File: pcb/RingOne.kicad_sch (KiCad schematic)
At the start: 23 parts

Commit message: Schema: add power path control, input button and bluetooth module
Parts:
- added BT?: 1S Li-Po, symbol Device:Battery_Cell
- added C? (x2): 4.7uF, symbol Device:C
- added C?: 100nF, symbol Device:C
- added C? (x7): 1uF, symbol Device:C
- added C? (x2): 1uF, Capacitor_SMD:C_0603_1608Metric, symbol Device:C
- added C?: 100nF, Capacitor_SMD:C_0603_1608Metric, symbol Device:C
- added D?: 3V3, Diode_SMD:D_SOD-523, symbol Device:D_Zener
- added D? (x2): D_Schottky, symbol Device:D_Schottky
- added D?: EADA25L, symbol Device:D_Schottky_Dual_CommonAnode_KKA
- added J?: PROG_CONN, TCY_connectors:Amphenol_10114828-11103LF_1x03_P1.25mm_Vertical, symbol Connector_Generic:Conn_01x03
- added J?: DBG_UART, TCY_connectors:Amphenol_10114828-11103LF_1x03_P1.25mm_Vertical, symbol Connector_Generic:Conn_01x03
- added Q? (x2): YJQ3400, TCY_IC:UDFN-6-2EP_2x2mm_P0.65mm_EP1x0.7mm, symbol TCY_transistors:YJQ3400
- added R? (x2): 10k, symbol Device:R
- added R? (x2): 1k, symbol Device:R
- added R? (x2): R, symbol Device:R
- added R?: 2k2, symbol Device:R
- added R?: 22k, symbol Device:R
- added SW?: WAKEUP, TCY_buttons_switches:EVQ-P7J01P, symbol Switch:SW_Push_Dual
- added SW?: BOOT, TCY_buttons_switches:KMT031NGJLHS, symbol Switch:SW_Push_Dual
- added U?: MIC94300, TCY_IC:MLF-4_1.2x1.6mm_P0.5_1EP_0.85x0.5mm, symbol TCY_IC:MIC94300
- added U? (x2): LM66100, Package_TO_SOT_SMD:SOT-363_SC-70-6, symbol TCY_power_management:LM66100
- added U? (x2): PMDPB70XP, TCY_IC:UDFN-6-2EP_2x2mm_P0.65mm_EP1x0.7mm, symbol TCY_transistors:PMDPB70XP
- added U?: MCP73831-2-OT, Package_TO_SOT_SMD:SOT-23-5, symbol Battery_Management:MCP73831-2-OT
- added U?: RN4871, RF_Module:Microchip_RN4871, symbol RF_Bluetooth:RN4871
- added U?: BQ297xy, Package_SON:WSON-6_1.5x1.5mm_P0.5mm, symbol Battery_Management:BQ297xy
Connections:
- net +3V3: now also U?.22 (VSYS), C?.1, C?.1, U?.14 (VBAT)
- net GND: now also U?.10 (GND), U?.13 (ADDR0), U?.25 (EP), U?.3 (VCONN), U?.4 (GND), U?.9 (EPAD), C?.2, C?.2, C?.2, C?.2, C?.2, C?.2, C?.2, C?.2, C?.2, C?.2, C?.2, C?.2, D?.2 (A), D?.3 (A), J?.1 (Pin_1), J?.1 (Pin_1), Q?.4 (S2), R?.2, R?.2, R?.2, R?.2, SW?.1, SW?.1, SW?.3, SW?.3, U?.13 (GND), U?.2 (GND), U?.2 (GND), U?.2 (GND), U?.2 (GND), U?.2 (VSS), U?.5 (E_PAD)
- net RESET: now also U?.10 (RST)
- net SCL: now also U?.8 (SDA)
- net SDA: now also U?.7 (SCL)
- net VBUS: now also U?.18 (VBUS_SENSE), C?.1, C?.1, U?.6, U?.7
- net CC1: now reaches U?.1 (CC1DB)
- net CC1: now also J?.A5 (CC1), U?.2 (CC1), D?.1 (K)
- net USB_VALID: now reaches U?.11 (VBUS_VALID)
- net USB_ATTACH: now reaches U?.12 (ATTACH)
- net USB_DEBUG: now reaches U?.14 (DEBUG1)
- net at U?.19 (VBUS_EN_SINK): now also R?.2
- net at U?.21 (VREG_1V2): now also C?.1
- net at U?.23 (VREG_2V7): now also C?.1
- net CC2: now reaches U?.4 (CC2)
- net CC2: now also J?.B5 (CC2), U?.5 (CC2DB), D?.2 (K)
- net at U?.6 (RESET): now also R?.1
- net USB_INT: now reaches U?.9 (ALERT#)
- net PWR_EN: now reaches U?.5 (EN)
- net PWR_EN: now also D?.1 (K), D?.1 (K), D?.1 (K), R?.1
- net VCC: now reaches U?.8 (VI)
- net VCC: now also C?.1, C?.1, U?.6 (VOUT), U?.6 (VOUT)
- new net: BT?.2 (-), C?.2, Q?.1 (S), U?.4 (VSS)
- new net: C?.1, R?.2, U?.5 (BAT)
- new net: R?.1, R?.2, U?.2, U?.5
- new net: R?.2, U?.3 (~CE), U?.5 (ST)
- new net: C?.1, U?.3 (VOUT)
- new net: C?.1, U?.4 (VIN)
- new net: R?.1, U?.1, U?.4
- new net: R?.1, U?.6 (V-)
- new net: Q?.2 (G1), U?.3 (Dout)
- new net: Q?.3 (D2), Q?.6 (D2), Q?.7 (D2), Q?.8 (D2)
- new net: Q?.5 (G2), U?.2 (Cout)
- new net: R?.1, U?.5 (PROG)
- new net +5V: C?.1, R?.1, U?.1 (VIN), U?.3, U?.4 (VDD), U?.8
- new net +BATT: BT?.1 (+), C?.1, R?.1, U?.1 (VIN), U?.3 (VBAT), U?.3 (~CE)
- new net BL_RX: U?.8 (UART_TX)
- new net BL_TX: U?.7 (UART_RX)
- new net BTN_Denoise_BOOT/IN: SW?.2, SW?.4
- new net BTN_Denoise_WAKE/IN: SW?.2, SW?.4
- new net DBG_RX: J?.3 (Pin_3)
- new net DBG_TX: J?.2 (Pin_2)
- new net PWR_BTN: D?.2 (A)
- new net PWR_MCU: D?.2 (A)
- new net P_OR: U?.5 (ST)
- new net SWCLK: J?.2 (Pin_2)
- new net SWDIO: J?.3 (Pin_3)
- no-connect marks 3 -> 15
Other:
- added sheet BTN_Denoise_BOOT (BTN_Denoise.kicad_sch)
- added sheet BTN_Denoise_WAKE (BTN_Denoise.kicad_sch)
- note added: "Battery protection"
- note added: "Charging"
- note added: "Charging current: 45 mA"
- note added: "Current sensing"
- note added: "IMU"
- note added: "Input buttons"
- note added: "Power OR-ing"
- note added: "Prog & debug"
- note added: "Use intenal pullup in MCU for: INT, DEBUG, VALID, ATTACH"
- moved on the sheet: C?, D?, FB?, J?, R?, SW?, TP?, U?, U?A

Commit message: Schema: finalization of schematic, break main page into hierarchical
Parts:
- removed BT?: 1S Li-Po, symbol Device:Battery_Cell
- removed C? (x2): 4.7uF, symbol Device:C
- removed C?: 100nF, symbol Device:C
- removed C? (x7): 1uF, symbol Device:C
- removed C? (x2): 1uF, Capacitor_SMD:C_0603_1608Metric, symbol Device:C
- removed C?: 100nF, Capacitor_SMD:C_0603_1608Metric, symbol Device:C
- removed D?: 3V3, Diode_SMD:D_SOD-523, symbol Device:D_Zener
- removed D? (x2): D_Schottky, symbol Device:D_Schottky
- removed D?: EADA25L, symbol Device:D_Schottky_Dual_CommonAnode_KKA
- removed FB?: 50R@100Mhz, Inductor_SMD:L_1206_3216Metric, symbol Device:FerriteBead_Small
- removed J?: USB_C_Receptacle_USB2.0, Connector_USB:USB_C_Receptacle_HRO_TYPE-C-31-M-12, symbol Connector:USB_C_Receptacle_USB2.0
- removed Q? (x2): YJQ3400, TCY_IC:UDFN-6-2EP_2x2mm_P0.65mm_EP1x0.7mm, symbol TCY_transistors:YJQ3400
- removed R? (x2): 10k, symbol Device:R
- removed R? (x2): 1k, symbol Device:R
- removed R? (x2): R, symbol Device:R
- removed R? (x2): 22R, Resistor_SMD:R_0603_1608Metric, symbol Device:R
- removed R?: 2k2, symbol Device:R
- removed R?: 22k, symbol Device:R
- removed SW?: WAKEUP, TCY_buttons_switches:EVQ-P7J01P, symbol Switch:SW_Push_Dual
- removed SW?: BOOT, TCY_buttons_switches:KMT031NGJLHS, symbol Switch:SW_Push_Dual
- removed TP?: VBUS, TCY_connectors:TestPoint_Pad_D0.5mm, symbol Connector:TestPoint
- removed U?: MIC94300, TCY_IC:MLF-4_1.2x1.6mm_P0.5_1EP_0.85x0.5mm, symbol TCY_IC:MIC94300
- removed U? (x2): LM66100, Package_TO_SOT_SMD:SOT-363_SC-70-6, symbol TCY_power_management:LM66100
- removed U? (x2): PMDPB70XP, TCY_IC:UDFN-6-2EP_2x2mm_P0.65mm_EP1x0.7mm, symbol TCY_transistors:PMDPB70XP
- removed U?: USBLC6-2SC6, Package_TO_SOT_SMD:SOT-23-6, symbol Power_Protection:USBLC6-2SC6
- removed U?: MCP73831-2-OT, Package_TO_SOT_SMD:SOT-23-5, symbol Battery_Management:MCP73831-2-OT
- removed U?: STUSB1600AQTR, Package_DFN_QFN:QFN-24-1EP_4x4mm_P0.5mm_EP2.7x2.7mm, symbol TCY_IC:STUSB1600AQTR
- removed U?: BQ297xy, Package_SON:WSON-6_1.5x1.5mm_P0.5mm, symbol Battery_Management:BQ297xy
- removed U?: NCV8165ML330, Package_DFN_QFN:DFN-8-1EP_3x3mm_P0.65mm_EP1.55x2.4mm, symbol TCY_voltage_regulators:NCV8165ML330
- added C1: 10uF, Capacitor_SMD:C_0805_2012Metric, symbol Device:C
- added C2, C3, C4, C5, C6: 100nF, Capacitor_SMD:C_0603_1608Metric, symbol Device:C
- C10, C9: renamed from C?; footprint (none) -> TCY_passives:C_0603_1608Metric
- J1, J2: renamed from J?; footprint TCY_connectors:Amphenol_10114828-11103LF_1x03_P1.25mm_Vertical -> TCY_connectors:Amphenol_10114830-11103LF_1x03_P1.25mm_Horizontal
- U4: renamed from U?; symbol TCY_IC:KTD2026BEWE -> TCY_LEDs:KTD2026BEWE
- gave numbers to parts that had none: 13
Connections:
- net +3V3: now also C1.1, C2.1, C3.1, C4.1, C5.1, C6.1; no longer U1.1 (VBAT)
- net BL_RX: now also U1.13 (PA3)
- net BL_TX: now also U1.12 (PA2)
- net DBG_RX: now also U1.22 (PB11)
- net DBG_TX: now also U1.21 (PB10)
- net GND: now also C1.2, C2.2, C3.2, C4.2, C5.2, C6.2
- net IMU_INT1: now also U1.25 (PB12)
- net IMU_INT2: now also U1.19 (PB1)
- net MISO: now also U1.27 (PB14)
- net MOSI: now also U1.28 (PB15)
- net PWR_BTN: now also U1.10 (PA0)
- net PWR_MCU: now also U1.17 (PA7)
- net RESET: now also U1.7 (NRST)
- net SCK: now also U1.26 (PB13)
- net SCL: now also U1.30 (PA9)
- net SDA: now also U1.31 (PA10)
- net SWCLK: now also U1.37 (PA14)
- net SWDIO: now also U1.34 (PA13)
- net USB_ATTACH: now also U1.40 (PB4)
- net USB_DEBUG: now also U1.42 (PB6)
- net USB_INT: now also U1.20 (PB2)
- net USB_VALID: now also U1.39 (PB3)
- net BAT_V_MON: now reaches U1.14 (PA4)
- net CS_MON: now reaches U1.15 (PA5)
- net BAT_M_EN: now reaches U1.16 (PA6)
- net CS_FLASH: now reaches U1.18 (PB0)
- net CS_FLASH: now also U6.1 (~CS)
- net PER_EN: now reaches U1.2 (PC13)
- net CS_IMU: now reaches U1.29 (PA8)
- net CS_IMU: now also U5.12 (MODE/CS)
- net USB_D+: now reaches U1.32 (PA11)
- net USB_D-: now reaches U1.33 (PA12)
- net PWR_OR: now reaches U1.38 (PA15)
- net CHARG_STAT: now reaches U1.45 (PB8)
- removed net CS: U5.12 (MODE/CS), U6.1 (~CS)
- net LED_PWR renamed PER_PWR
- no-connect marks 15 -> 21
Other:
- removed sheet BTN_Denoise_BOOT
- removed sheet BTN_Denoise_WAKE
- added sheet Battery_management (Battery_management.kicad_sch)
- added sheet Power_management (Power_management.kicad_sch)
- added sheet USB-C (USB-C.kicad_sch)
- note removed: "Battery protection"
- note removed: "Charging"
- note removed: "Charging current: 45 mA"
- note removed: "Current sensing"
- note removed: "Input buttons"
- note removed: "Power OR-ing"
- note removed: "USB type-C input"
- note removed: "Use intenal pullup in MCU for: INT, DEBUG, VALID, ATTACH"
- moved on the sheet: C7, J1, J2, R1, R2, SW1, U1, U2

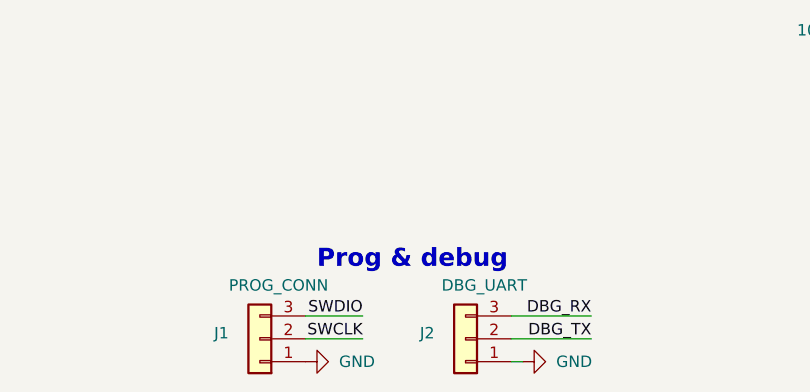
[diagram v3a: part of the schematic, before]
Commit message: PCB: add connection of connector mounting point to ground
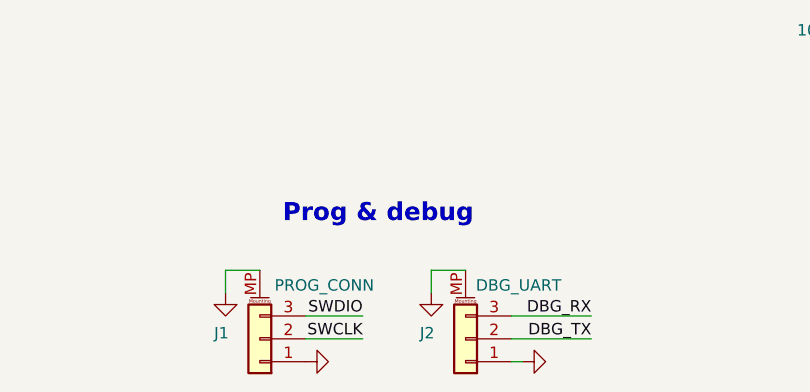
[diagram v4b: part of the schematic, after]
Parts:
- J1, J2: symbol Connector_Generic:Conn_01x03 -> Connector_Generic_MountingPin:Conn_01x03_MountingPin
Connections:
- net GND: now also J1.MP (MountPin), J2.MP (MountPin)
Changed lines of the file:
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@@
+    (stroke (width 0) (type solid) (color 0 0 0 0))
+  )
+  (wire (pts (xy 127 177.8) (xy 130.81 177.8))
+    (stroke (width 0) (type solid) (color 0 0 0 0))
+  )
+  (wire (pts (xy 127 180.34) (xy 127 177.8))
     (stroke (width 0) (type solid) (color 0 0 0 0))
   )
@@
   )
   (wire (pts (xy 149.86 40.64) (xy 149.86 38.1))
+    (stroke (width 0) (type solid) (color 0 0 0 0))
+  )
+  (wire (pts (xy 149.86 177.8) (xy 153.67 177.8))
+    (stroke (width 0) (type solid) (color 0 0 0 0))
+  )
+  (wire (pts (xy 149.86 180.34) (xy 149.86 177.8))
     (stroke (width 0) (type solid) (color 0 0 0 0))
   )
@@
     (stroke (width 0) (type dash) (color 0 0 0 0))
   )
-  (text "Prog & debug" (at 137.16 177.8 0)
+  (text "Prog & debug" (at 133.35 172.72 0)
     (effects (font (size 2 2) (thickness 0.4) bold) (justify left bottom))
   )
@@
     )
   )
+  (symbol (lib_id "power:GND") (at 127 180.34 0) (unit 1)
+    (in_bom yes) (on_board yes)
+    (property "Reference" "#PWR0198" (id 0) (at 127 186.69 0)
+      (effects (font (size 1.27 1.27)) hide)
+    )
+    (property "Value" "GND" (id 1) (at 127 186.055 90)
+      (effects (font (size 1.27 1.27)) hide)
+    )
+    (property "Footprint" "" (id 2) (at 127 180.34 0)
+      (effects (font (size 1.27 1.27)) hide)
+    )
+    (property "Datasheet" "" (id 3) (at 127 180.34 0)
+      (effects (font (size 1.27 1.27)) hide)
+    )
+  )
   (symbol (lib_id "power:GND") (at 135.89 187.96 90) (unit 1)
     (in_bom yes) (on_board yes)
@@
       (effects (font (size 1.27 1.27)) hide)
     )
-    (property "Value" "GND" (id 1) (at 141.605 187.96 90))
+    (property "Value" "GND" (id 1) (at 141.605 187.96 90)
+      (effects (font (size 1.27 1.27)) hide)
+    )
     (property "Footprint" "" (id 2) (at 135.89 187.96 0)
       (effects (font (size 1.27 1.27)) hide)
@@
     )
   )
+  (symbol (lib_id "power:GND") (at 149.86 180.34 0) (unit 1)
+    (in_bom yes) (on_board yes)
+    (property "Reference" "#PWR0197" (id 0) (at 149.86 186.69 0)
+      (effects (font (size 1.27 1.27)) hide)
+    )
+    (property "Value" "GND" (id 1) (at 149.86 186.055 90)
+      (effects (font (size 1.27 1.27)) hide)
+    )
+    (property "Footprint" "" (id 2) (at 149.86 180.34 0)
+      (effects (font (size 1.27 1.27)) hide)
+    )
+    (property "Datasheet" "" (id 3) (at 149.86 180.34 0)
+      (effects (font (size 1.27 1.27)) hide)
+    )
+  )
   (symbol (lib_id "power:GND") (at 160.02 187.96 90) (unit 1)
     (in_bom yes) (on_board yes)
@@
       (effects (font (size 1.27 1.27)) hide)
     )
-    (property "Value" "GND" (id 1) (at 165.735 187.96 90))
+    (property "Value" "GND" (id 1) (at 165.735 187.96 90)
+      (effects (font (size 1.27 1.27)) hide)
+    )
     (property "Footprint" "" (id 2) (at 160.02 187.96 0)
       (effects (font (size 1.27 1.27)) hide)
@@
     )
   )
-  (symbol (lib_id "Connector_Generic:Conn_01x03") (at 130.81 185.42 180) (unit 1)
+  (symbol (lib_id "Connector_Generic_MountingPin:Conn_01x03_MountingPin") (at 130.81 185.42 180) (unit 1)
     (in_bom yes) (on_board yes)
     (property "Reference" "J1" (id 0) (at 126.5428 184.785 0))
-    (property "Value" "PROG_CONN" (id 1) (at 132.893 179.476 0))
+    (property "Value" "PROG_CONN" (id 1) (at 137.973 179.476 0))
     (property "Footprint" "TCY_connectors:Amphenol_10114830-11103LF_1x03_P1.25mm_Horizontal" (id 2) (at 130.81 185.42 0)
       (effects (font (size 1.27 1.27)) hide)
@@
     )
   )
-  (symbol (lib_id "Connector_Generic:Conn_01x03") (at 153.67 185.42 180) (unit 1)
+  (symbol (lib_id "Connector_Generic_MountingPin:Conn_01x03_MountingPin") (at 153.67 185.42 180) (unit 1)
     (in_bom yes) (on_board yes)
     (property "Reference" "J2" (id 0) (at 149.4028 184.785 0))
-    (property "Value" "DBG_UART" (id 1) (at 155.7528 179.4764 0))
+    (property "Value" "DBG_UART" (id 1) (at 159.5628 179.4764 0))
     (property "Footprint" "TCY_connectors:Amphenol_10114830-11103LF_1x03_P1.25mm_Horizontal" (id 2) (at 153.67 185.42 0)
       (effects (font (size 1.27 1.27)) hide)
@@
     (stroke (width 0.001) (type solid) (color 132 0 132 1))
     (fill (color 72 72 72 1.0000))
-    (property "Název listu" "Battery_management" (id 0) (at 31.75 69.2141 0)
+    (property "Sheet name" "Battery_management" (id 0) (at 31.75 69.2141 0)
       (effects (font (size 1.27 1.27)) (justify left bottom))
     )
@@
     (stroke (width 0.001) (type solid) (color 132 0 132 1))
     (fill (color 72 72 72 1.0000))
-    (property "Název listu" "Power_management" (id 0) (at 31.75 112.3941 0)
+    (property "Sheet name" "Power_management" (id 0) (at 31.75 112.3941 0)
       (effects (font (size 1.27 1.27)) (justify left bottom))
     )
@@
     (stroke (width 0.001) (type solid) (color 132 0 132 1))
     (fill (color 72 72 72 1.0000))
-    (property "Název listu" "USB-C" (id 0) (at 31.75 27.3041 0)
+    (property "Sheet name" "USB-C" (id 0) (at 31.75 27.3041 0)
       (effects (font (size 1.27 1.27)) (justify left bottom))
     )
@@
       (reference "#PWR0195") (unit 1) (value "GND") (footprint "")
     )
+    (path "/f0a1fa42-faf3-4521-acd4-9fe59a2915cd"
+      (reference "#PWR0197") (unit 1) (value "GND") (footprint "")
+    )
+    (path "/21d0263a-7281-437e-b015-69943e84731b"
+      (reference "#PWR0198") (unit 1) (value "GND") (footprint "")
+    )
     (path "/bda31249-ab3b-4aa0-9b2e-986fe291b91e"
       (reference "C1") (unit 1) (value "10uF") (footprint "Capacitor_SMD:C_0805_2012Metric")
@@
       (reference "#PWR0166") (unit 1) (value "GND") (footprint "")
     )
+    (path "/d4a7e79c-9128-4fa4-80c8-5ed7650db9b6/12be52e6-3c44-4354-993f-f098502fb45b"
+      (reference "#PWR0199") (unit 1) (value "GND") (footprint "")
+    )
     (path "/d4a7e79c-9128-4fa4-80c8-5ed7650db9b6/745dbf74-bff4-4801-8f72-08ba815e8ed8"

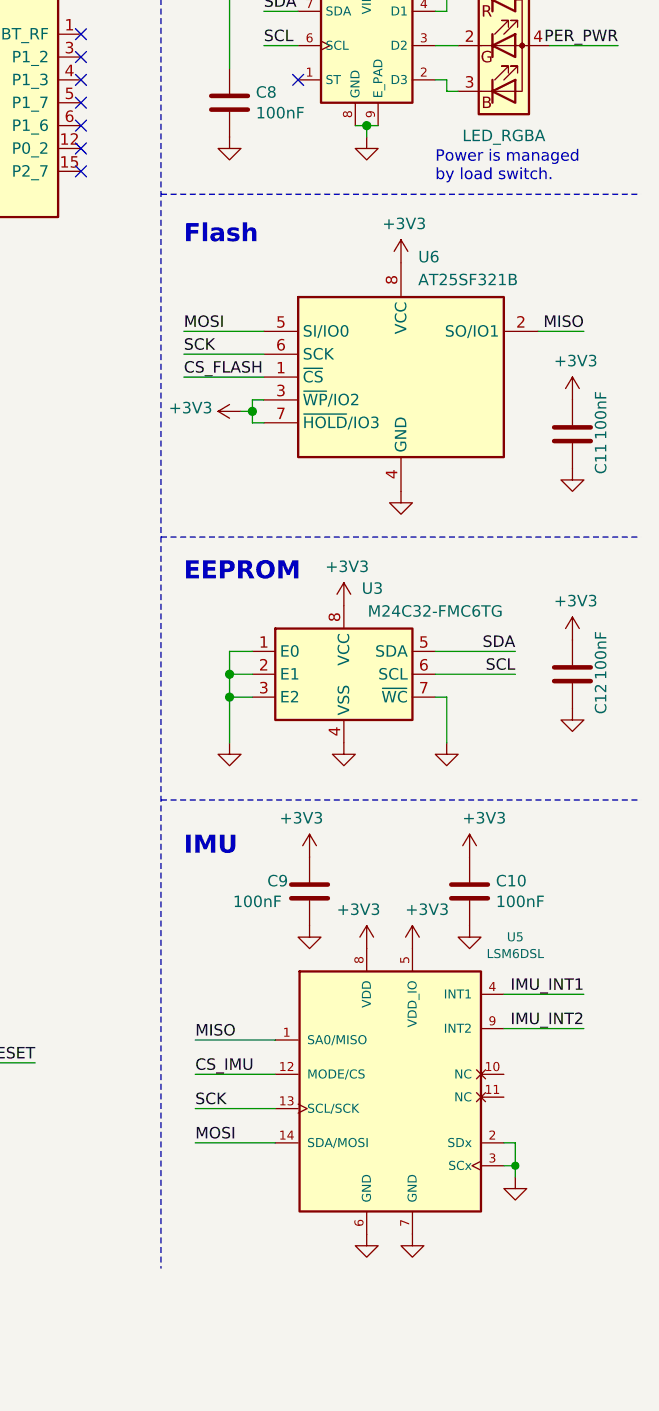
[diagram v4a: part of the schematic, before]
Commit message: Schema & PCB: Update page layout, add notes about SPI modes and I2C addresses
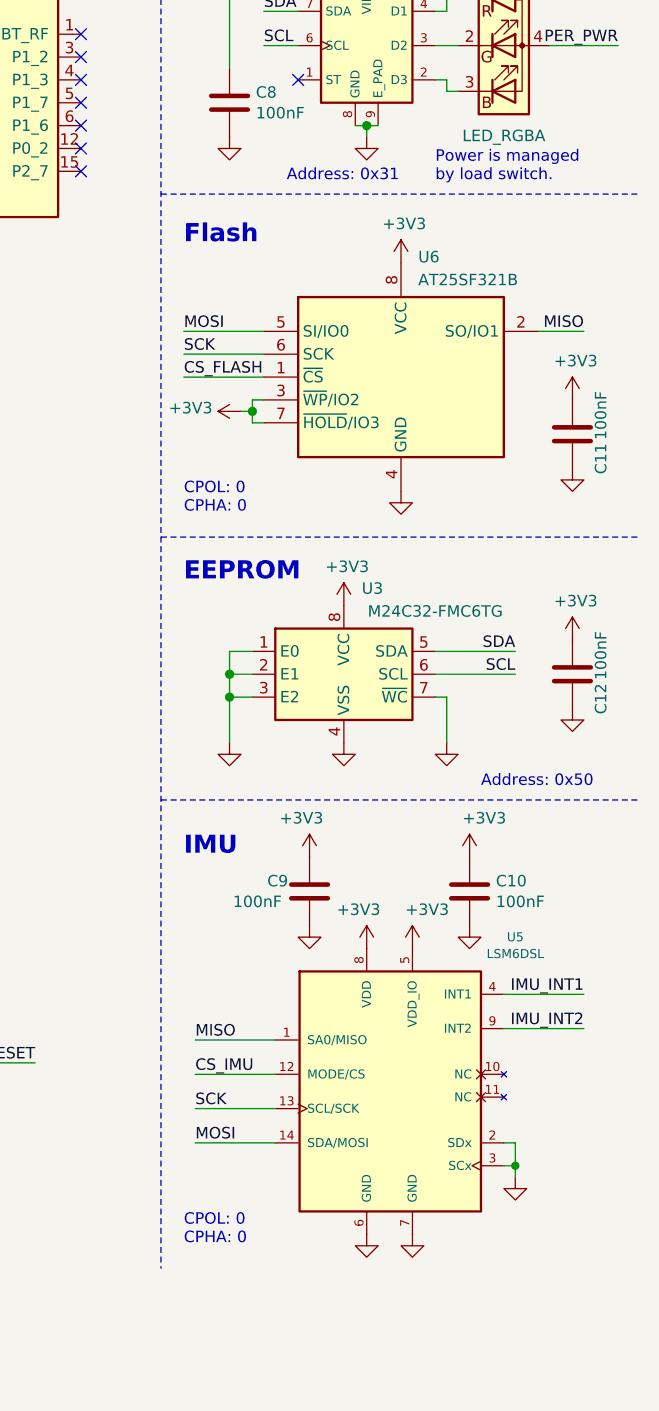
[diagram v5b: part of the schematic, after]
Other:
- note added: "Address: 0x31"
- note added: "Address: 0x50"
- note added: "CPOL: 0 CPHA: 0"
